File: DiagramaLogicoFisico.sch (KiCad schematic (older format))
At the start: 41 parts, among them J1 Conn_01x02_Servo1, J10 Conn_01x04_TRIS, J2 Conn_01x03_UART1, J3 Conn_01x03_UART2, J4 Conn_01x04_PWM, J5 Conn_01x05_PROGRAMER, J6 Conn_01x02_POWER, J7 Conn_01x02_Servo2, J8 Conn_01x02_Servo3, J9 Conn_01x02_Servo4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

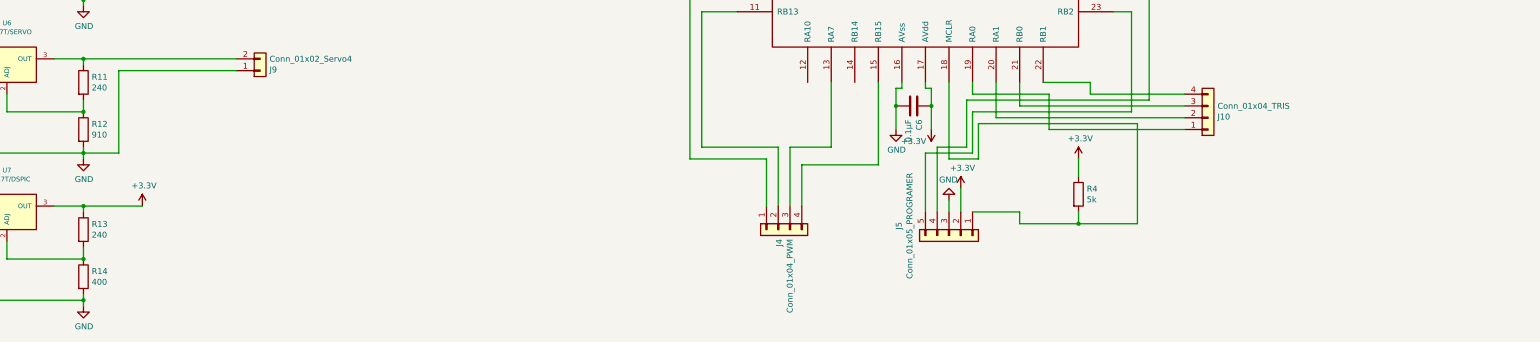
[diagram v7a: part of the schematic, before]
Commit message: Añadido puerto tris y clema extra
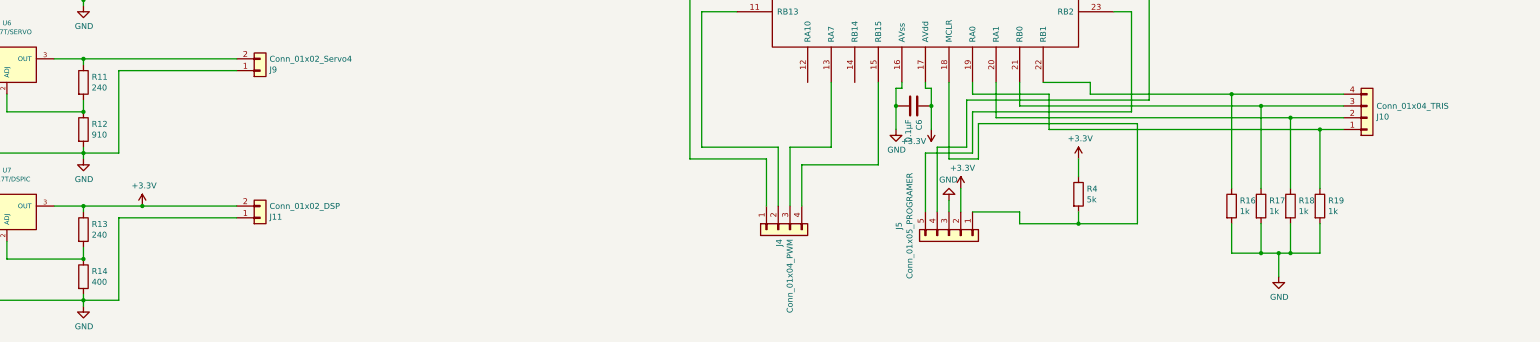
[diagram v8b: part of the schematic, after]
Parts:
- added J11: Conn_01x02_DSP, TerminalBlock:TerminalBlock_bornier-2_P5.08mm, symbol Connector_Generic:Conn_01x02
- added R16, R17, R18, R19: 1k, Resistor_THT:R_Axial_DIN0204_L3.6mm_D1.6mm_P5.08mm_Horizontal, symbol Device:R
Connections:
- net +3V3: now also J11.2 (Pin_2)
- net GND: now also J11.1 (Pin_1), R16.2, R17.2, R18.2, R19.2
- net at J10.1 (Pin_1), U2.19 (RA0): now also R19.1
- net at J10.2 (Pin_2), U2.20 (RA1): now also R18.1
- net at J10.3 (Pin_3), U2.21 (RB0): now also R17.1
- net at J10.4 (Pin_4), U2.22 (RB1): now also R16.1
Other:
- moved on the sheet: J10
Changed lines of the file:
@@
 	18250 13500 18250 12650
-Wire Wire Line
-	16900 13500 18250 13500
 Wire Wire Line
 	16900 13850 16900 13500
@@
 	1    0    0    -1
 $EndComp
-$Comp
-L Device:R R4
-U 1 1 5E81C5AF
-P 17800 14200
-F 0 "R4" H 17870 14246 50  0000 L CNN
-F 1 "5k" H 17870 14155 50  0000 L CNN
-F 2 "Resistor_THT:R_Axial_DIN0204_L3.6mm_D1.6mm_P5.08mm_Horizontal" V 17730 14200 50  0001 C CNN
-F 3 "~" H 17800 14200 50  0001 C CNN
-	1    17800 14200
-	1    0    0    -1
-$EndComp
 Wire Wire Line
 	17800 13900 17800 14050
@@
 Wire Wire Line
 	16950 13600 16950 13900
-Wire Wire Line
-	18300 13600 16950 13600
 $Comp
 L power:GND #PWR0104
@@
 	1    0    0    1
 $EndComp
+Wire Wire Line
+	9350 10350 10650 10350
+Wire Wire Line
+	9350 11150 9650 11150
+Wire Wire Line
+	9650 11150 9650 10450
+Wire Wire Line
+	9650 10450 10650 10450
+Wire Wire Line
+	9350 11750 10650 11750
+Wire Wire Line
+	9350 12550 9650 12550
+Wire Wire Line
+	9650 12550 9650 11850
+Wire Wire Line
+	9650 11850 10650 11850
+Wire Wire Line
+	9350 13050 10650 13050
+Wire Wire Line
+	9350 13850 9650 13850
+Wire Wire Line
+	9650 13850 9650 13150
+Wire Wire Line
+	9650 13150 10650 13150
+Wire Wire Line
+	16900 13250 16900 13350
+Wire Wire Line
+	16900 13350 17550 13350
+Wire Wire Line
+	17550 13350 17550 13650
+Wire Wire Line
+	17100 13250 17100 13550
+Wire Wire Line
+	17300 13250 17300 13450
+Wire Wire Line
+	17500 13250 17900 13250
+Wire Wire Line
+	17900 13250 17900 13350
+Wire Wire Line
+	16900 13500 18250 13500
+$Comp
+L Device:R R4
+U 1 1 5E81C5AF
+P 17800 14200
+F 0 "R4" H 17870 14246 50  0000 L CNN
+F 1 "5k" H 17870 14155 50  0000 L CNN
+F 2 "Resistor_THT:R_Axial_DIN0204_L3.6mm_D1.6mm_P5.08mm_Horizontal" V 17730 14200 50  0001 C CNN
+F 3 "~" H 17800 14200 50  0001 C CNN
+	1    17800 14200
+	1    0    0    -1
+$EndComp
+Wire Wire Line
+	18300 13600 16950 13600
+$Comp
+L Connector_Generic:Conn_01x04 J10
+U 1 1 5EB8B1CB
+P 20250 13550
+F 0 "J10" H 20330 13542 50  0000 L CNN
+F 1 "Conn_01x04_TRIS" H 20330 13451 50  0000 L CNN
+F 2 "Connector_PinHeader_2.54mm:PinHeader_1x04_P2.54mm_Vertical" H 20250 13550 50  0001 C CNN
+F 3 "~" H 20250 13550 50  0001 C CNN
+	1    20250 13550
+	1    0    0    1
+$EndComp
+Wire Wire Line
+	17900 13350 19100 13350
+Wire Wire Line
+	17300 13450 19350 13450
+Wire Wire Line
+	17100 13550 19600 13550
 $Comp
 L Connector_Generic:Conn_01x02 J9
@@
 	1    0    0    1
 $EndComp
-Wire Wire Line
-	9350 10350 10650 10350
-Wire Wire Line
-	9350 11150 9650 11150
-Wire Wire Line
-	9650 11150 9650 10450
-Wire Wire Line
-	9650 10450 10650 10450
-Wire Wire Line
-	9350 11750 10650 11750
-Wire Wire Line
-	9350 12550 9650 12550
-Wire Wire Line
-	9650 12550 9650 11850
-Wire Wire Line
-	9650 11850 10650 11850
-Wire Wire Line
-	9350 13050 10650 13050
-Wire Wire Line
-	9350 13850 9650 13850
-Wire Wire Line
-	9650 13850 9650 13150
-Wire Wire Line
-	9650 13150 10650 13150
-Wire Wire Line
-	16900 13250 16900 13350
-Wire Wire Line
-	16900 13350 17550 13350
-Wire Wire Line
-	17550 13350 17550 13650
-Wire Wire Line
-	17550 13650 18700 13650
-Wire Wire Line
-	17100 13250 17100 13550
-Wire Wire Line
-	17300 13250 17300 13450
-Wire Wire Line
-	17300 13450 18700 13450
-Wire Wire Line
-	17500 13250 17900 13250
-Wire Wire Line
-	17900 13250 17900 13350
-Wire Wire Line
-	17900 13350 18700 13350
-$Comp
-L Connector_Generic:Conn_01x04 J10
-U 1 1 5EB8B1CB
-P 18900 13550
-F 0 "J10" H 18980 13542 50  0000 L CNN
-F 1 "Conn_01x04_TRIS" H 18980 13451 50  0000 L CNN
-F 2 "Connector_PinHeader_2.54mm:PinHeader_1x04_P2.54mm_Vertical" H 18900 13550 50  0001 C CNN
-F 3 "~" H 18900 13550 50  0001 C CNN
-	1    18900 13550
+$Comp
+L Connector_Generic:Conn_01x02 J11
+U 1 1 5ECACDB4
+P 10850 14400
+F 0 "J11" H 10930 14392 50  0000 L CNN
+F 1 "Conn_01x02_DSP" H 10930 14301 50  0000 L CNN
+F 2 "TerminalBlock:TerminalBlock_bornier-2_P5.08mm" H 10850 14400 50  0001 C CNN
+F 3 "~" H 10850 14400 50  0001 C CNN
+	1    10850 14400
 	1    0    0    1
 $EndComp
 Wire Wire Line
-	17100 13550 18700 13550
+	9850 14300 10650 14300
+Connection ~ 9850 14300
+Wire Wire Line
+	9350 15100 9650 15100
+Wire Wire Line
+	9650 15100 9650 14400
+Wire Wire Line
+	9650 14400 10650 14400
+Wire Wire Line
+	17550 13650 19850 13650
+$Comp
+L power:GND #PWR0102
+U 1 1 5ED1E4A7
+P 19500 14900
+F 0 "#PWR0102" H 19500 14650 50  0001 C CNN
+F 1 "GND" H 19505 14727 50  0000 C CNN
+F 2 "" H 19500 14900 50  0001 C CNN
+F 3 "" H 19500 14900 50  0001 C CNN
+	1    19500 14900
+	1    0    0    -1
+$EndComp
+$Comp
+L Device:R R16
+U 1 1 5ED2CC60
+P 19100 14300
+F 0 "R16" H 19170 14346 50  0000 L CNN
+F 1 "1k" H 19170 14255 50  0000 L CNN
+F 2 "Resistor_THT:R_Axial_DIN0204_L3.6mm_D1.6mm_P5.08mm_Horizontal" V 19030 14300 50  0001 C CNN
+F 3 "~" H 19100 14300 50  0001 C CNN
+	1    19100 14300
+	1    0    0    -1
+$EndComp
+$Comp
+L Device:R R17
+U 1 1 5ED3A919
+P 19350 14300
+F 0 "R17" H 19420 14346 50  0000 L CNN
+F 1 "1k" H 19420 14255 50  0000 L CNN
+F 2 "Resistor_THT:R_Axial_DIN0204_L3.6mm_D1.6mm_P5.08mm_Horizontal" V 19280 14300 50  0001 C CNN
+F 3 "~" H 19350 14300 50  0001 C CNN
+	1    19350 14300
+	1    0    0    -1
+$EndComp
+$Comp
+L Device:R R18
+U 1 1 5ED485EB
+P 19600 14300
+F 0 "R18" H 19670 14346 50  0000 L CNN
+F 1 "1k" H 19670 14255 50  0000 L CNN
+F 2 "Resistor_THT:R_Axial_DIN0204_L3.6mm_D1.6mm_P5.08mm_Horizontal" V 19530 14300 50  0001 C CNN
+F 3 "~" H 19600 14300 50  0001 C CNN
+	1    19600 14300
+	1    0    0    -1
+$EndComp
+Wire Wire Line
+	19500 14700 19350 14700
+Wire Wire Line
+	19100 14700 19100 14450
+Wire Wire Line
+	19350 14450 19350 14700
+Connection ~ 19350 14700
+Wire Wire Line
+	19350 14700 19100 14700
+Wire Wire Line
+	19500 14700 19600 14700
+Wire Wire Line
+	19600 14700 19600 14450
+Connection ~ 19500 14700
+Wire Wire Line
+	19600 14700 19850 14700
+Connection ~ 19600 14700
+Wire Wire Line
+	19500 14700 19500 14900
+Wire Wire Line
+	19100 14150 19100 13350
+Connection ~ 19100 13350
+Wire Wire Line
+	19100 13350 20050 13350
+Wire Wire Line
+	19350 14150 19350 13450
+Connection ~ 19350 13450
+Wire Wire Line
+	19350 13450 20050 13450
+Wire Wire Line
+	19600 14150 19600 13550
+Connection ~ 19600 13550
+Wire Wire Line
+	19600 13550 20050 13550
+Wire Wire Line
+	19850 14700 19850 14450
+$Comp
+L Device:R R19
+U 1 1 5ED562FD
+P 19850 14300
+F 0 "R19" H 19920 14346 50  0000 L CNN
+F 1 "1k" H 19920 14255 50  0000 L CNN
+F 2 "Resistor_THT:R_Axial_DIN0204_L3.6mm_D1.6mm_P5.08mm_Horizontal" V 19780 14300 50  0001 C CNN
+F 3 "~" H 19850 14300 50  0001 C CNN
+	1    19850 14300
+	1    0    0    -1
+$EndComp
+Wire Wire Line
+	19850 14150 19850 13650
+Connection ~ 19850 13650
+Wire Wire Line
+	19850 13650 20050 13650
 $EndSCHEMATC
